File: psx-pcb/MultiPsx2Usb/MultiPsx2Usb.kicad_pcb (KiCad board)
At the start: 2 copper layers, 1 part

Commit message: Rough schematic mockup done. need to create test circuits and see what works and what doesn't.
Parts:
- moved AVR32DU1 59.0 mm to (144.7, 148.1)
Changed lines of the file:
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@@
 	(footprint "avr32du:SOIC-14"
 		(layer "F.Cu")
-		(at 142.67 89.145)
+		(at 144.67 148.145)
 		(property "Reference" "AVR32DU1"
 			(at -5.61 0 90)

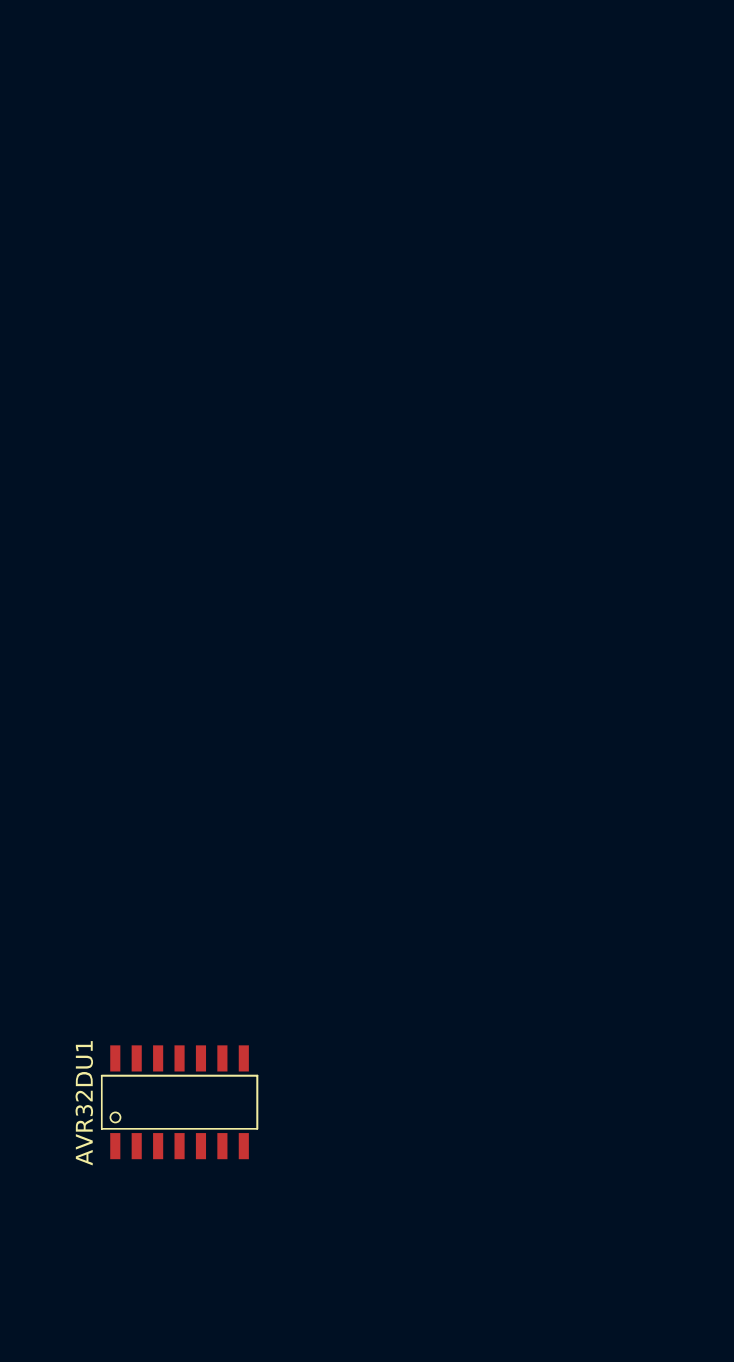
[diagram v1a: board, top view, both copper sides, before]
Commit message: Populated PCB, finished adding everything I should need
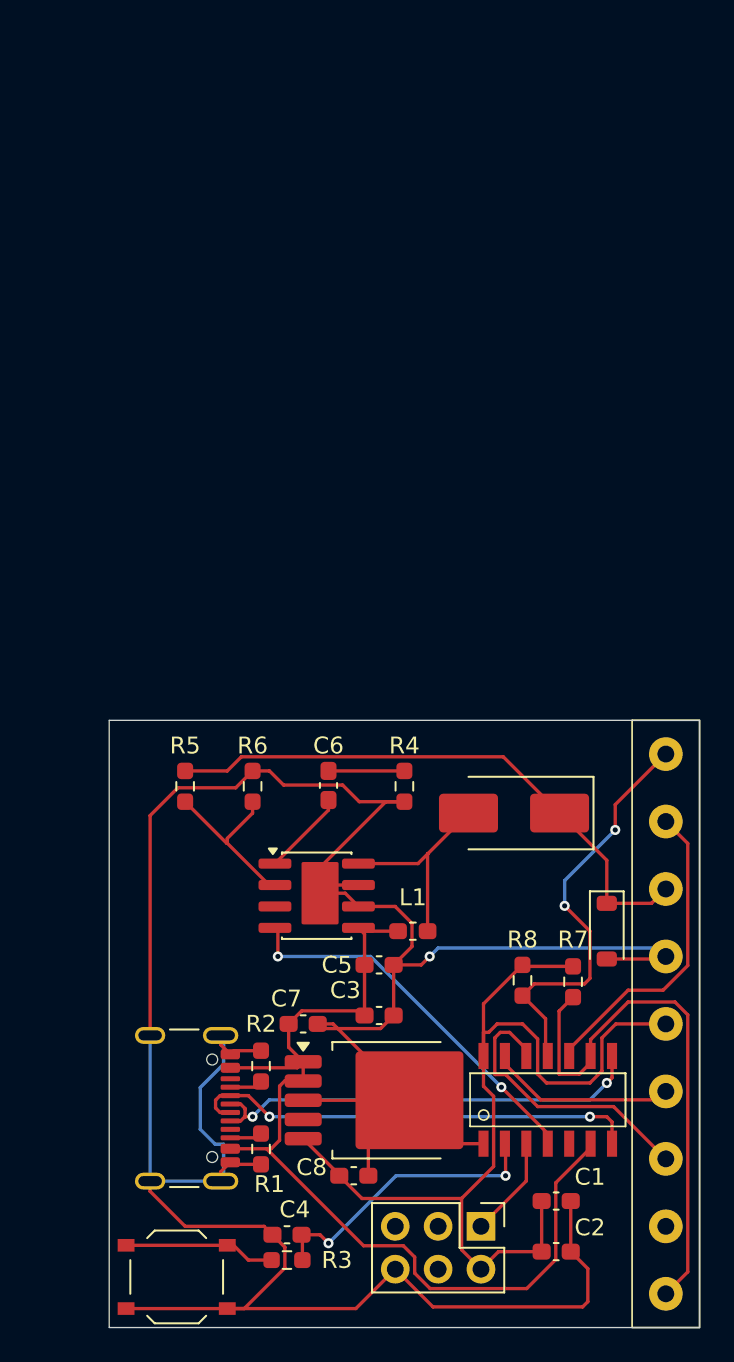
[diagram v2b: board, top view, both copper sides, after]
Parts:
- added C1: 10 nF, Capacitor_SMD:C_0603_1608Metric_Pad1.08x0.95mm_HandSolder, F.Cu at (167.0, 154.0)
- added C2: 100 nF, Capacitor_SMD:C_0603_1608Metric_Pad1.08x0.95mm_HandSolder, F.Cu at (167.0, 157.0)
- added C3: 0.1 uF, Capacitor_SMD:C_0603_1608Metric_Pad1.08x0.95mm_HandSolder, F.Cu at (156.5, 143.0)
- added C4: 100 nF, Capacitor_SMD:C_0603_1608Metric_Pad1.08x0.95mm_HandSolder, F.Cu at (151.0, 156.0)
- added C5: 22 uF, Capacitor_SMD:C_0603_1608Metric_Pad1.08x0.95mm_HandSolder, F.Cu at (156.5, 140.0)
- added C6: 0.1 uF, Capacitor_SMD:C_0603_1608Metric_Pad1.08x0.95mm_HandSolder, F.Cu at (153.5, 129.4)
- added C7: 10 uF, Capacitor_SMD:C_0603_1608Metric_Pad1.08x0.95mm_HandSolder, F.Cu at (152.0, 143.5)
- added C8: 10 uF, Capacitor_SMD:C_0603_1608Metric_Pad1.08x0.95mm_HandSolder, F.Cu at (155.0, 152.5)
- added D1: MBRS120T3G, Diode_SMD:D_SMB_Handsoldering, F.Cu at (164.5, 131.0)
- added D2: 1N5819, Diode_SMD:D_SOD-123, F.Cu at (170.0, 138.0)
- added J1: AVR-UPDI-6, Connector_PinHeader_2.54mm:PinHeader_2x03_P2.54mm_Vertical, F.Cu at (162.5, 155.5)
- added J2: USB_C_Receptacle_USB2.0_14P, Connector_USB:USB_C_Receptacle_GCT_USB4105-xx-A_16P_TopMnt_Horizontal, F.Cu at (144.0, 148.5)
- added L1: 22 uH, Inductor_SMD:L_0603_1608Metric_Pad1.05x0.95mm_HandSolder, F.Cu at (158.5, 138.0)
- added NCV5171: ~, Package_SO:SOIC-8-1EP_3.9x4.9mm_P1.27mm_EP2.41x3.81mm_ThermalVias, F.Cu at (152.8, 135.9)
- added PS2_CON1: ~, avr32du:PS2_CONNECTOR, F.Cu at (173.5, 143.5)
- added R1: 5.1k, Resistor_SMD:R_0603_1608Metric_Pad0.98x0.95mm_HandSolder, F.Cu at (149.5, 150.9)
- added R2: 5.1k, Resistor_SMD:R_0603_1608Metric_Pad0.98x0.95mm_HandSolder, F.Cu at (149.5, 146.0)
- added R3: 330, Resistor_SMD:R_0603_1608Metric_Pad0.98x0.95mm_HandSolder, F.Cu at (151.0, 157.5)
- added R4: 5K, Resistor_SMD:R_0603_1608Metric_Pad0.98x0.95mm_HandSolder, F.Cu at (158.0, 129.4)
- added R5: 48.7k, Resistor_SMD:R_0603_1608Metric_Pad0.98x0.95mm_HandSolder, F.Cu at (145.0, 129.4)
- added R6: 10k, Resistor_SMD:R_0603_1608Metric_Pad0.98x0.95mm_HandSolder, F.Cu at (149.0, 129.4)
- added R7: 1k, Resistor_SMD:R_0603_1608Metric_Pad0.98x0.95mm_HandSolder, F.Cu at (168.0, 141.0)
- added R8: R, Resistor_SMD:R_0603_1608Metric_Pad0.98x0.95mm_HandSolder, F.Cu at (165.0, 140.9)
- added SW1: SW_Push, Button_Switch_SMD:SW_Push_1P1T_XKB_TS-1187A, F.Cu at (144.5, 158.5)
- added U1: AP7583Q, Package_TO_SOT_SMD:TO-252-5_TabPin3, F.Cu at (157.0, 148.0)
- moved AVR32DU1 21.8 mm to (166.5, 148.0)
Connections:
- AVR32DU1 pad 1: unconnected-(AVR32DU1-GND-Pad1) -> GND
- AVR32DU1 pad 10: unconnected-(AVR32DU1-PD4-Pad10) -> Net-(AVR32DU1-PD4)
- AVR32DU1 pad 11: unconnected-(AVR32DU1-PD5-Pad11) -> Net-(AVR32DU1-PD5)
- AVR32DU1 pad 12: unconnected-(AVR32DU1-PD6-Pad12) -> Net-(AVR32DU1-PD6)
- AVR32DU1 pad 13: unconnected-(AVR32DU1-PD7-Pad13) -> Net-(AVR32DU1-PD7)
- AVR32DU1 pad 14: unconnected-(AVR32DU1-VDD-Pad14) -> +3V3
- AVR32DU1 pad 2: unconnected-(AVR32DU1-RESET-Pad2) -> Net-(AVR32DU1-RESET)
- AVR32DU1 pad 3: unconnected-(AVR32DU1-UPDI-Pad3) -> Net-(AVR32DU1-UPDI)
- AVR32DU1 pad 4: unconnected-(AVR32DU1-PA0-Pad4) -> /SS
- AVR32DU1 pad 6: unconnected-(AVR32DU1-VUSB-Pad6) -> +5V
- AVR32DU1 pad 7: unconnected-(AVR32DU1-DM-Pad7) -> Net-(AVR32DU1-DM)
- AVR32DU1 pad 8: unconnected-(AVR32DU1-DP-Pad8) -> Net-(AVR32DU1-DP)
- AVR32DU1 pad 9: unconnected-(AVR32DU1-PC3-Pad9) -> Net-(AVR32DU1-PC3)
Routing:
- net GND: track 0.00 -> 189.5 mm, vias 0 -> 1
- net +3V3: track 0.00 -> 59.2 mm
- net +5V: track 0.00 -> 59.0 mm
- net +7.5V: track 0.00 -> 33.8 mm
- net Net-(AVR32DU1-PC3): track 0.00 -> 32.5 mm
- net Net-(AVR32DU1-DM): track 0.00 -> 27.0 mm, vias 0 -> 2
- net Net-(AVR32DU1-DP): track 0.00 -> 26.4 mm, vias 0 -> 2
- net Net-(AVR32DU1-PD5): track 0.00 -> 24.8 mm, vias 0 -> 2
- net /SS: track 0.00 -> 22.7 mm, vias 0 -> 2
- net Net-(AVR32DU1-PD4): track 0.00 -> 19.2 mm
- net Net-(AVR32DU1-RESET): track 0.00 -> 17.4 mm, vias 0 -> 2
- net Net-(AVR32DU1-PD6): track 0.00 -> 17.2 mm
- net /V_SW: track 0.00 -> 12.4 mm
- net Net-(AVR32DU1-PD7): track 0.00 -> 11.6 mm
- net Net-(NCV5171-FB): track 0.00 -> 10.5 mm
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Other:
- board outline added: 35 x 36 mm

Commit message: Finished designing the PCB, track widths have been set for all net classes, still need to fix GND track width
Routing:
- net +5V: track 59.0 -> 51.6 mm, vias 0 -> 4
- net (no net): vias 0 -> 1

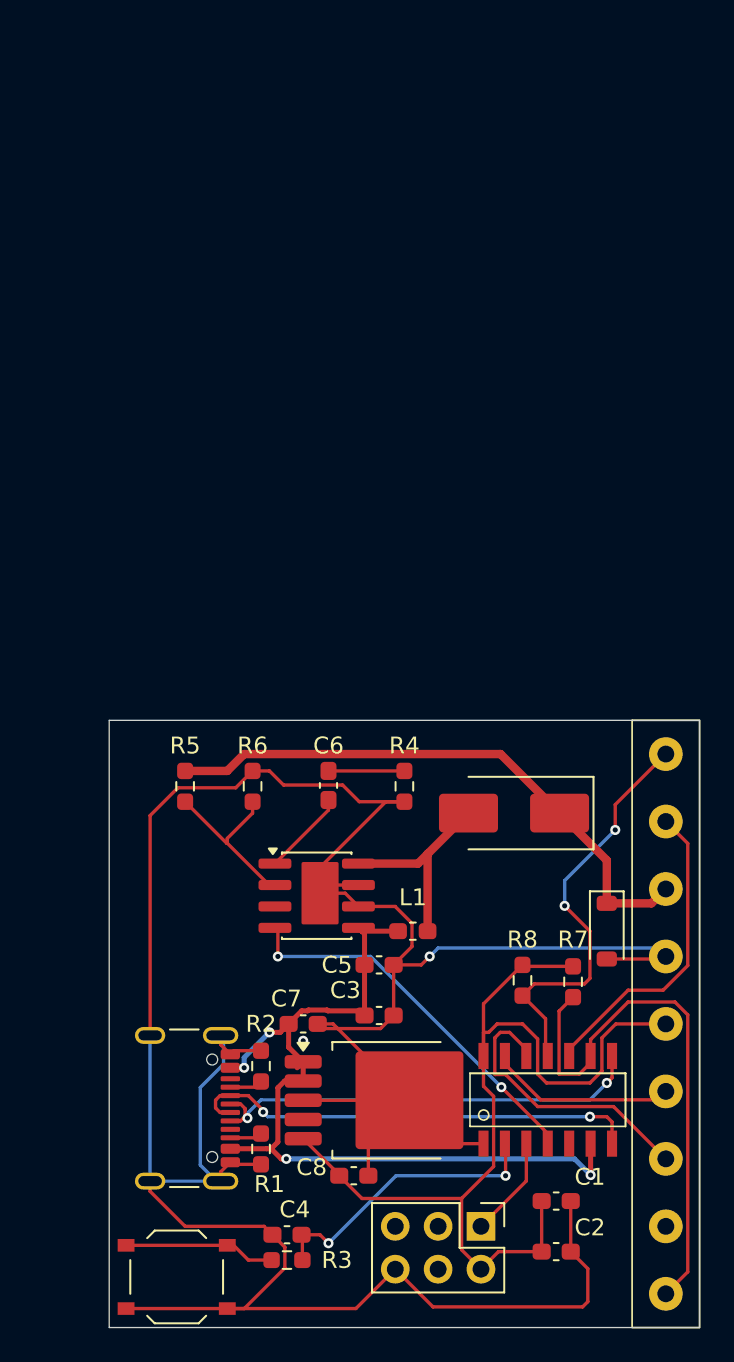
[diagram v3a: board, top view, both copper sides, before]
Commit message: fixed inductor footprint. added 6-pin FTDI header. connected V_USB to 3.3V instead of 5V.
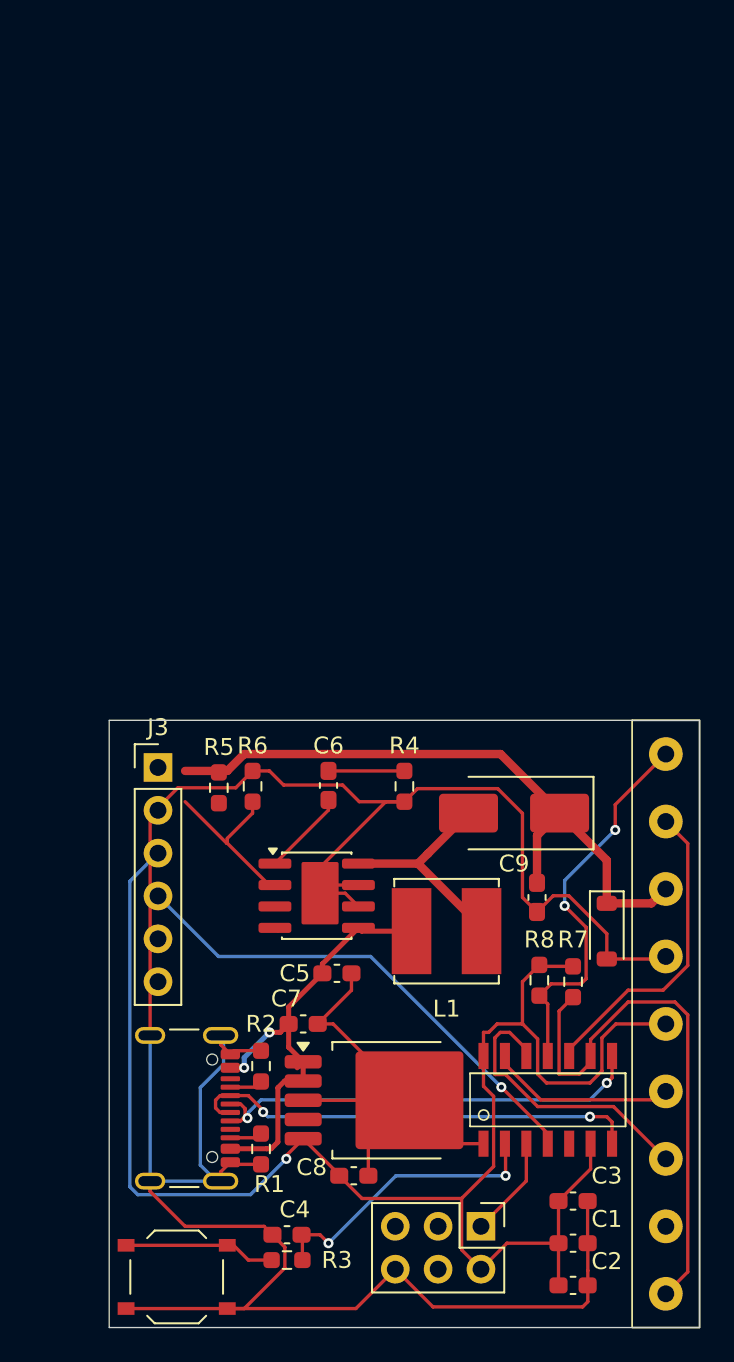
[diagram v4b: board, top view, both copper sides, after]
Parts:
- added C9: 22 uF, Capacitor_SMD:C_0603_1608Metric_Pad1.08x0.95mm_HandSolder, F.Cu at (165.9, 136.0)
- added J3: UART, Connector_PinHeader_2.54mm:PinHeader_1x06_P2.54mm_Vertical, F.Cu at (143.4, 128.3)
- AVR16DU14: renamed from AVR32DU1; value ~ -> AVR16DU14
- L1: footprint Inductor_SMD:L_0603_1608Metric_Pad1.05x0.95mm_HandSolder -> Inductor_SMD:L_Bourns_SRN6045TA
- R8: value R -> 1k
- moved C3 15.9 mm to (168.0, 154.0)
- moved C1 2.69 mm to (168.0, 156.5)
- moved C5 2.55 mm to (154.0, 140.5)
- moved C2 2.24 mm to (168.0, 159.0)
- moved R5 2.00 mm to (147.0, 129.5)
- moved L1 2.00 mm to (160.5, 138.0)
- moved R8 1.00 mm to (166.0, 140.9)
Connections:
- AVR16DU14 pad 4: /SS -> /TxD
- AVR16DU14 pad 6: +5V -> +3V3
- C3 pad 1: +5V -> +3V3
- NCV5171 pad 4: /SS -> unconnected-(NCV5171-SS-Pad4)
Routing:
- net +3V3: track 59.2 -> 96.0 mm, vias 0 -> 1
- net /TxD: track 0.00 -> 29.5 mm, vias 0 -> 1
- net +5V: track 51.6 -> 27.2 mm, vias 4 -> 2
- net /SS: track 22.7 -> 0.00 mm, vias 2 -> 0
- net GND: track 189.5 -> 183.9 mm, vias 1 -> 0
- net +7.5V: track 33.9 -> 38.6 mm
- net Net-(AVR16DU14-PD5): track 24.8 -> 23.3 mm
- net /V_SW: track 12.4 -> 13.4 mm
- net (no net): vias 1 -> 0

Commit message: Added circuitry to allow for serial TX, which is switchable with a microswitch to USB CC pin voltage measurement. Added player 2 ATT pin support
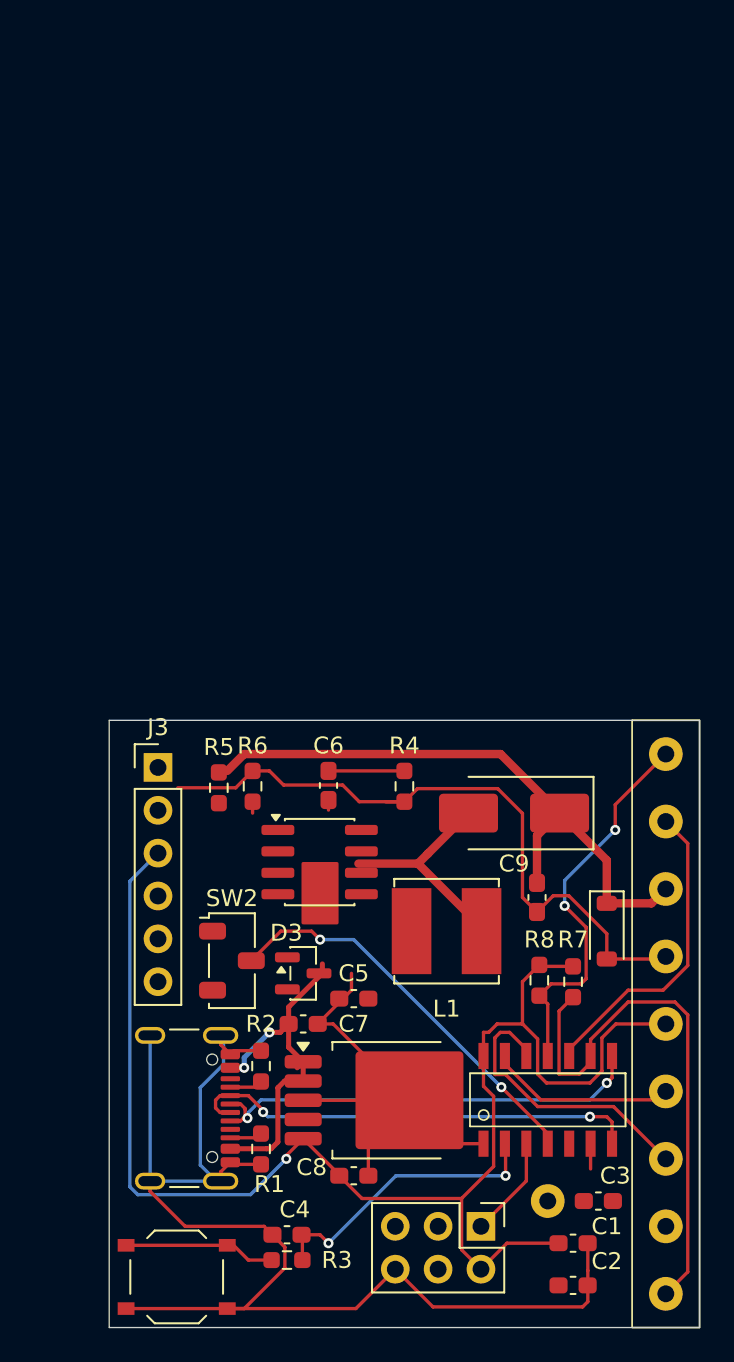
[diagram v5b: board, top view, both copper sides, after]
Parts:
- added D3: BAT54C, Package_TO_SOT_SMD:SOT-23, F.Cu at (152.0, 140.5)
- added J4: ~, avr32du:PS2_P2, F.Cu at (166.5, 154.0)
- added SW2: SW_Nidec_CAS-120A1, Button_Switch_SMD:Nidec_Copal_CAS-120A, F.Cu at (147.8, 139.8)
- moved NCV5171 2.00 mm to (153.0, 133.9)
- moved C5 1.80 mm to (155.0, 142.0)
- moved C3 1.50 mm to (169.5, 154.0)
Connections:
- AVR16DU14 pad 4: /TxD -> /<NO NET>
- AVR16DU14 pad 5: unconnected-(AVR16DU14-PA1-Pad5) -> /P2_ATT
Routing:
- net /TxD: track 29.5 -> 0.00 mm, vias 1 -> 0
- net GND: track 183.9 -> 155.8 mm
- net /<NO NET>: track 0.00 -> 23.9 mm, vias 0 -> 2
- net Net-(NCV5171-FB): track 10.5 -> 0.68 mm
- net +3V3: track 96.0 -> 88.3 mm
- net +5V: track 27.2 -> 21.7 mm
- net Net-(NCV5171-VC): track 5.09 -> 0.59 mm
- net +7.5V: track 38.6 -> 36.1 mm
